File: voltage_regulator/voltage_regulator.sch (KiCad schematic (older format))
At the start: 6 parts, among them Q1 BC548, U2 LM317AT

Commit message: Design update
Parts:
- removed C4: 100u, symbol voltage_regulator-rescue:C
- removed Q1: BC548, TO-92, symbol voltage_regulator-rescue:BC548
- removed R3: 240, symbol voltage_regulator-rescue:R
- removed R4: 2k78, symbol voltage_regulator-rescue:R
- removed R5: 1, symbol voltage_regulator-rescue:R
- removed U2: LM317AT, TO-220, symbol voltage_regulator-rescue:LM317AT
- added C1: 100u, symbol Device:C
- added P1: PWR_IN, symbol power_sources:PWR_IN
- added Q1: BC548, Package_TO_SOT_THT:TO-92_Inline, symbol Transistor_BJT:BC548
- added R1: 240, symbol Device:R
- added R2: 2k78, symbol Device:R
- added R3: 1, symbol Device:R
- added R4: 180k, symbol Device:R
- added U1: LM317_3PinPackage, symbol Regulator_Linear:LM317_3PinPackage
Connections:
- net labels added: OUTPUT_14V4_N, OUTPUT_14V4_P
- net labels removed: OUTPUT_14.4V_N, OUTPUT_14.4V_P
- wire segments 20 -> 31
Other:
- note added: ".include power.cir\n.tran 10us 500us uic"

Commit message: Schematic update
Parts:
- removed C1: 100u, symbol Device:C
- R2: value 2k78 -> 3k117
- R4: value 180k -> 30
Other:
- note added: ".include power.cir\n.tran 10us 1ms uic"
- note removed: ".include power.cir\n.tran 10us 500us uic"
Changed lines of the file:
@@
 	5700 3150 6000 3150
 Connection ~ 6000 3150
-Wire Wire Line
-	6400 1950 6400 2350
-Connection ~ 6400 1950
-Wire Wire Line
-	6400 2650 6400 3150
-Connection ~ 6400 3150
 Wire Notes Line
 	4300 4200 4300 1550
 Wire Wire Line
-	6000 1950 6400 1950
-Wire Wire Line
 	5400 3700 5400 3900
 Wire Wire Line
 	6000 3150 6000 3300
-Wire Wire Line
-	6000 3150 6400 3150
-Wire Wire Line
-	6400 1950 6900 1950
-Wire Wire Line
-	6400 3150 6900 3150
 $Comp
 L Regulator_Linear:LM317_3PinPackage U1
@@
 P 6000 2700
 F 0 "R2" H 6070 2746 50  0000 L CNN
-F 1 "2k78" H 6070 2655 50  0000 L CNN
+F 1 "3k117" H 6070 2655 50  0000 L CNN
 F 2 "" V 5930 2700 50  0001 C CNN
 F 3 "~" H 6000 2700 50  0001 C CNN
@@
 F 3 "~" H 6000 3450 50  0001 C CNN
 	1    6000 3450
-	1    0    0    -1
-$EndComp
-$Comp
-L Device:C C1
-U 1 1 5BE96820
-P 6400 2500
-F 0 "C1" H 6515 2546 50  0000 L CNN
-F 1 "100u" H 6515 2455 50  0000 L CNN
-F 2 "" H 6438 2350 50  0001 C CNN
-F 3 "~" H 6400 2500 50  0001 C CNN
-	1    6400 2500
 	1    0    0    -1
 $EndComp
@@
 	7000 4200 4300 4200
 Text Notes 7100 1700 0    50   ~ 0
-.include power.cir\n.tran 10us 500us uic
+.include power.cir\n.tran 10us 1ms uic
 $Comp
 L Device:R R4
@@
 P 8100 2450
 F 0 "R4" H 8170 2496 50  0000 L CNN
-F 1 "180k" H 8170 2405 50  0000 L CNN
+F 1 "30" H 8170 2405 50  0000 L CNN
 F 2 "" V 8030 2450 50  0001 C CNN
 F 3 "~" H 8100 2450 50  0001 C CNN
@@
 Wire Wire Line
 	5400 2450 5400 2950
+Wire Wire Line
+	6000 1950 6900 1950
+Wire Wire Line
+	6000 3150 6900 3150
 $EndSCHEMATC

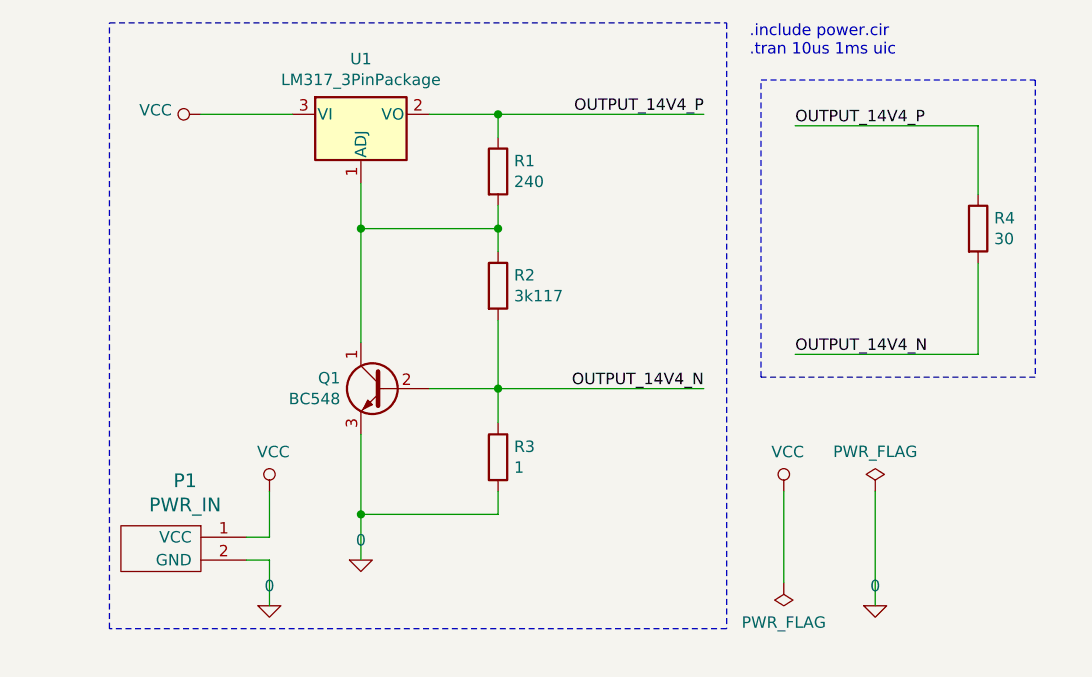
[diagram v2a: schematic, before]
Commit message: Capacitors added
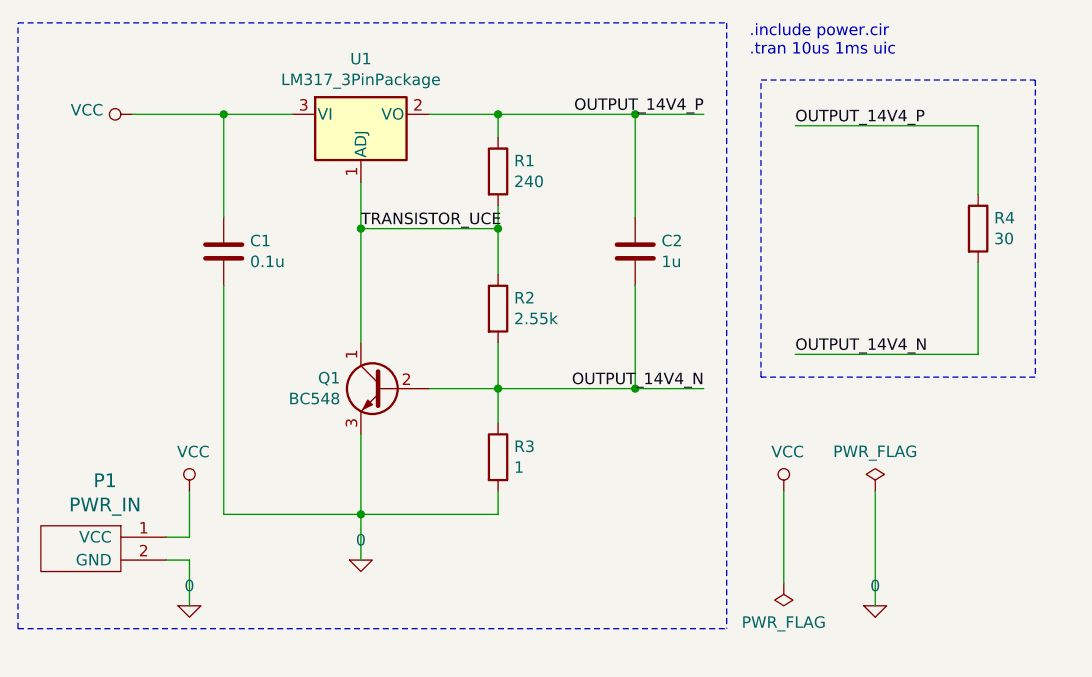
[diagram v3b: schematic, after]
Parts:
- added C1: 0.1u, symbol Device:C
- added C2: 1u, symbol Device:C
- R2: value 3k117 -> 2.55k
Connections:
- net 0: now also C1.2
- net OUTPUT_14V4_N: now also C2.2
- net OUTPUT_14V4_P: now also C2.1
- net VCC: now also C1.1
- net TRANSISTOR_UCE: now reaches Q1.1 (C), R1.2, R2.1, U1.1 (ADJ)
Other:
- moved on the sheet: P1, R2
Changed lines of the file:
@@
 	6000 2350 6000 2450
-Wire Wire Line
-	6000 2850 6000 3150
 Wire Wire Line
 	6000 3600 6000 3700
@@
 	5700 3150 6000 3150
 Connection ~ 6000 3150
-Wire Notes Line
-	4300 4200 4300 1550
 Wire Wire Line
 	5400 3700 5400 3900
@@
 L Device:R R2
 U 1 1 5BE963F2
-P 6000 2700
-F 0 "R2" H 6070 2746 50  0000 L CNN
-F 1 "3k117" H 6070 2655 50  0000 L CNN
-F 2 "" V 5930 2700 50  0001 C CNN
-F 3 "~" H 6000 2700 50  0001 C CNN
-	1    6000 2700
+P 6000 2800
+F 0 "R2" H 6070 2846 50  0000 L CNN
+F 1 "2.55k" H 6070 2755 50  0000 L CNN
+F 2 "" V 5930 2800 50  0001 C CNN
+F 3 "~" H 6000 2800 50  0001 C CNN
+	1    6000 2800
 	1    0    0    -1
 $EndComp
@@
 L power:VCC #PWR01
 U 1 1 5BE96D3C
-P 4700 1950
-F 0 "#PWR01" H 4700 1800 50  0001 C CNN
-F 1 "VCC" V 4718 2077 50  0000 L CNN
-F 2 "" H 4700 1950 50  0001 C CNN
-F 3 "" H 4700 1950 50  0001 C CNN
-	1    4700 1950
+P 4400 1950
+F 0 "#PWR01" H 4400 1800 50  0001 C CNN
+F 1 "VCC" V 4418 2077 50  0000 L CNN
+F 2 "" H 4400 1950 50  0001 C CNN
+F 3 "" H 4400 1950 50  0001 C CNN
+	1    4400 1950
 	0    -1   -1   0
 $EndComp
@@
 	-1   0    0    1
 $EndComp
-Wire Wire Line
-	4700 1950 5100 1950
 Wire Wire Line
 	5700 1950 6000 1950
@@
 L power_sources:PWR_IN P1
 U 1 1 5BE980A3
-P 4500 3700
-F 0 "P1" H 4631 3847 60  0000 C CNN
-F 1 "PWR_IN" H 4631 3741 60  0000 C CNN
-F 2 "" H 4500 3700 60  0001 C CNN
-F 3 "" H 4500 3700 60  0001 C CNN
-F 4 "X" H 4500 3700 50  0001 C CNN "Spice_Primitive"
-F 5 "PWR_IN" H 4500 3700 50  0001 C CNN "Spice_Model"
-F 6 "Y" H 4500 3700 50  0001 C CNN "Spice_Netlist_Enabled"
-	1    4500 3700
+P 4150 3700
+F 0 "P1" H 4281 3847 60  0000 C CNN
+F 1 "PWR_IN" H 4281 3741 60  0000 C CNN
+F 2 "" H 4150 3700 60  0001 C CNN
+F 3 "" H 4150 3700 60  0001 C CNN
+F 4 "X" H 4150 3700 50  0001 C CNN "Spice_Primitive"
+F 5 "PWR_IN" H 4150 3700 50  0001 C CNN "Spice_Model"
+F 6 "Y" H 4150 3700 50  0001 C CNN "Spice_Netlist_Enabled"
+	1    4150 3700
 	1    0    0    -1
 $EndComp
@@
 L power:VCC #PWR02
 U 1 1 5BE98134
-P 5000 3600
-F 0 "#PWR02" H 5000 3450 50  0001 C CNN
-F 1 "VCC" H 5017 3773 50  0000 C CNN
-F 2 "" H 5000 3600 50  0001 C CNN
-F 3 "" H 5000 3600 50  0001 C CNN
-	1    5000 3600
+P 4650 3600
+F 0 "#PWR02" H 4650 3450 50  0001 C CNN
+F 1 "VCC" H 4667 3773 50  0000 C CNN
+F 2 "" H 4650 3600 50  0001 C CNN
+F 3 "" H 4650 3600 50  0001 C CNN
+	1    4650 3600
 	1    0    0    -1
 $EndComp
@@
 L pspice:0 #GND01
 U 1 1 5BE98417
-P 5000 4100
-F 0 "#GND01" H 5000 4000 50  0001 C CNN
-F 1 "0" H 5000 4187 50  0000 C CNN
-F 2 "" H 5000 4100 50  0001 C CNN
-F 3 "~" H 5000 4100 50  0001 C CNN
-	1    5000 4100
-	1    0    0    -1
-$EndComp
-Wire Wire Line
-	4900 3800 5000 3800
-Wire Wire Line
-	5000 3800 5000 3600
-Wire Wire Line
-	4900 3900 5000 3900
-Wire Wire Line
-	5000 3900 5000 4100
-Wire Notes Line
-	4300 1550 7000 1550
+P 4650 4100
+F 0 "#GND01" H 4650 4000 50  0001 C CNN
+F 1 "0" H 4650 4187 50  0000 C CNN
+F 2 "" H 4650 4100 50  0001 C CNN
+F 3 "~" H 4650 4100 50  0001 C CNN
+	1    4650 4100
+	1    0    0    -1
+$EndComp
+Wire Wire Line
+	4550 3800 4650 3800
+Wire Wire Line
+	4650 3800 4650 3600
+Wire Wire Line
+	4550 3900 4650 3900
+Wire Wire Line
+	4650 3900 4650 4100
 Wire Notes Line
 	7000 1550 7000 4200
-Wire Notes Line
-	7000 4200 4300 4200
 Text Notes 7100 1700 0    50   ~ 0
 .include power.cir\n.tran 10us 1ms uic
@@
 	6000 2450 5400 2450
 Connection ~ 6000 2450
-Wire Wire Line
-	6000 2450 6000 2550
 Connection ~ 5400 2450
 Wire Wire Line
 	5400 2450 5400 2950
 Wire Wire Line
-	6000 1950 6900 1950
-Wire Wire Line
-	6000 3150 6900 3150
+	6000 1950 6600 1950
+Wire Wire Line
+	6000 3150 6600 3150
+Wire Wire Line
+	6000 2450 6000 2650
+Wire Wire Line
+	6000 2950 6000 3150
+Text Label 5400 2450 0    50   ~ 0
+TRANSISTOR_UCE
+$Comp
+L Device:C C1
+U 1 1 5C37AFDC
+P 4800 2550
+F 0 "C1" H 4915 2596 50  0000 L CNN
+F 1 "0.1u" H 4915 2505 50  0000 L CNN
+F 2 "" H 4838 2400 50  0001 C CNN
+F 3 "~" H 4800 2550 50  0001 C CNN
+	1    4800 2550
+	1    0    0    -1
+$EndComp
+$Comp
+L Device:C C2
+U 1 1 5C37B656
+P 6600 2550
+F 0 "C2" H 6715 2596 50  0000 L CNN
+F 1 "1u" H 6715 2505 50  0000 L CNN
+F 2 "" H 6638 2400 50  0001 C CNN
+F 3 "~" H 6600 2550 50  0001 C CNN
+	1    6600 2550
+	1    0    0    -1
+$EndComp
+Wire Wire Line
+	5400 3700 4800 3700
+Wire Wire Line
+	4800 3700 4800 2700
+Wire Wire Line
+	4800 2400 4800 1950
+Connection ~ 4800 1950
+Wire Wire Line
+	4800 1950 5100 1950
+Wire Wire Line
+	6600 2700 6600 3150
+Connection ~ 6600 3150
+Wire Wire Line
+	6600 3150 6900 3150
+Wire Wire Line
+	6600 2400 6600 1950
+Connection ~ 6600 1950
+Wire Wire Line
+	6600 1950 6900 1950
+Wire Notes Line
+	3900 4200 3900 1550
+Wire Notes Line
+	3900 1550 7000 1550
+Wire Notes Line
+	3900 4200 7000 4200
+Wire Wire Line
+	4400 1950 4800 1950
 $EndSCHEMATC
